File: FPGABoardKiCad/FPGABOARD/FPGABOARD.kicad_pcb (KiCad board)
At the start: 2 copper layers, 1 part, among them U1 ICE40HX1K-VQ100

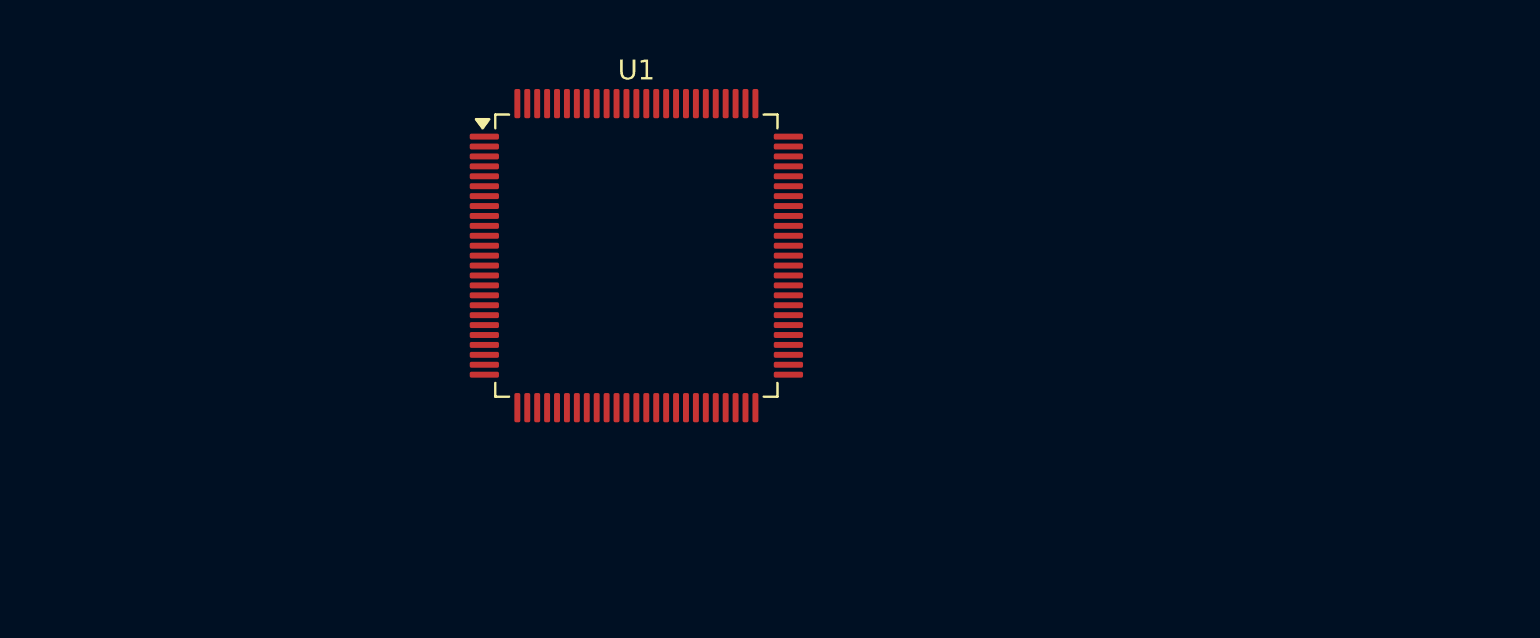
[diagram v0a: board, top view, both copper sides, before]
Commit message: FT2232 Wiring
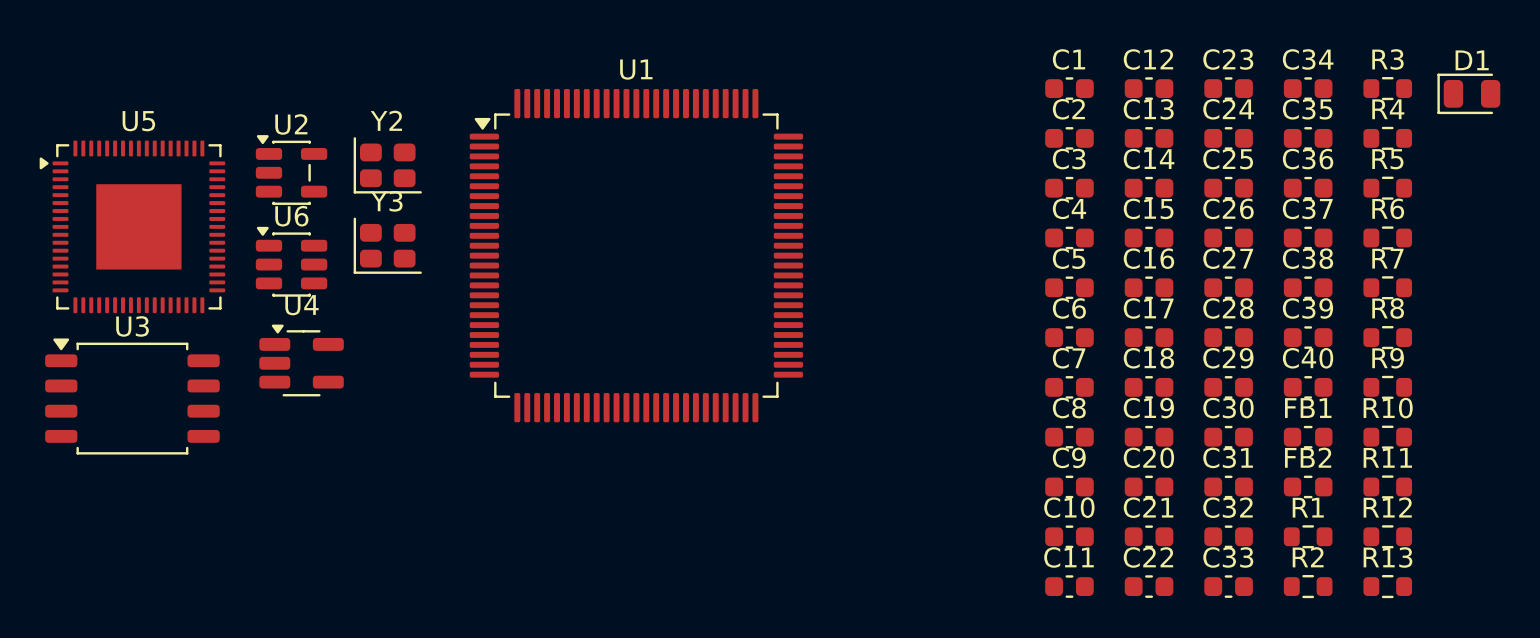
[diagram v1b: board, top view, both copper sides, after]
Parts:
- added C1: 4.7u, Capacitor_SMD:C_0603_1608Metric, F.Cu at (187.4, 94.6)
- added C10: 100n, Capacitor_SMD:C_0603_1608Metric, F.Cu at (187.4, 117.1)
- added C11: 100n, Capacitor_SMD:C_0603_1608Metric, F.Cu at (187.4, 119.7)
- added C12: 100n, Capacitor_SMD:C_0603_1608Metric, F.Cu at (191.4, 94.6)
- added C13: 10u, Capacitor_SMD:C_0603_1608Metric, F.Cu at (191.4, 97.1)
- added C14: 100n, Capacitor_SMD:C_0603_1608Metric, F.Cu at (191.4, 99.6)
- added C15: 100n, Capacitor_SMD:C_0603_1608Metric, F.Cu at (191.4, 102.1)
- added C16: 100n, Capacitor_SMD:C_0603_1608Metric, F.Cu at (191.4, 104.6)
- added C17: 100n, Capacitor_SMD:C_0603_1608Metric, F.Cu at (191.4, 107.1)
- added C18: 100n, Capacitor_SMD:C_0603_1608Metric, F.Cu at (191.4, 109.6)
- added C19: 100n, Capacitor_SMD:C_0603_1608Metric, F.Cu at (191.4, 112.1)
- added C2: 4.7u, Capacitor_SMD:C_0603_1608Metric, F.Cu at (187.4, 97.1)
- added C20: 100n, Capacitor_SMD:C_0603_1608Metric, F.Cu at (191.4, 114.6)
- added C21: 100n, Capacitor_SMD:C_0603_1608Metric, F.Cu at (191.4, 117.1)
- added C22: 100n, Capacitor_SMD:C_0603_1608Metric, F.Cu at (191.4, 119.7)
- added C23: 10u, Capacitor_SMD:C_0603_1608Metric, F.Cu at (195.4, 94.6)
- added C24: 10u, Capacitor_SMD:C_0603_1608Metric, F.Cu at (195.4, 97.1)
- added C25: 100n, Capacitor_SMD:C_0603_1608Metric, F.Cu at (195.4, 99.6)
- added C26: 100n, Capacitor_SMD:C_0603_1608Metric, F.Cu at (195.4, 102.1)
- added C27: 100n, Capacitor_SMD:C_0603_1608Metric, F.Cu at (195.4, 104.6)
- added C28: 100n, Capacitor_SMD:C_0603_1608Metric, F.Cu at (195.4, 107.1)
- added C29: 100n, Capacitor_SMD:C_0603_1608Metric, F.Cu at (195.4, 109.6)
- added C3: 4.7u, Capacitor_SMD:C_0603_1608Metric, F.Cu at (187.4, 99.6)
- added C30: 100n, Capacitor_SMD:C_0603_1608Metric, F.Cu at (195.4, 112.1)
- added C31: 100n, Capacitor_SMD:C_0603_1608Metric, F.Cu at (195.4, 114.6)
- added C32: 100n, Capacitor_SMD:C_0603_1608Metric, F.Cu at (195.4, 117.1)
- added C33: 100n, Capacitor_SMD:C_0603_1608Metric, F.Cu at (195.4, 119.7)
- added C34: 100n, Capacitor_SMD:C_0603_1608Metric, F.Cu at (199.4, 94.6)
- added C35: 10u, Capacitor_SMD:C_0603_1608Metric, F.Cu at (199.4, 97.1)
- added C36: 100n, Capacitor_SMD:C_0603_1608Metric, F.Cu at (199.4, 99.6)
- added C37: 100n, Capacitor_SMD:C_0603_1608Metric, F.Cu at (199.4, 102.1)
- added C38: 100n, Capacitor_SMD:C_0603_1608Metric, F.Cu at (199.4, 104.6)
- added C39: 100n, Capacitor_SMD:C_0603_1608Metric, F.Cu at (199.4, 107.1)
- added C4: 4.7u, Capacitor_SMD:C_0603_1608Metric, F.Cu at (187.4, 102.1)
- added C40: 10u, Capacitor_SMD:C_0603_1608Metric, F.Cu at (199.4, 109.6)
- added C5: 10u, Capacitor_SMD:C_0603_1608Metric, F.Cu at (187.4, 104.6)
- added C6: 100n, Capacitor_SMD:C_0603_1608Metric, F.Cu at (187.4, 107.1)
- added C7: 100n, Capacitor_SMD:C_0603_1608Metric, F.Cu at (187.4, 109.6)
- added C8: 100n, Capacitor_SMD:C_0603_1608Metric, F.Cu at (187.4, 112.1)
- added C9: 100n, Capacitor_SMD:C_0603_1608Metric, F.Cu at (187.4, 114.6)
- added D1: DONE, LED_SMD:LED_0805_2012Metric, F.Cu at (207.7, 94.8)
- added FB1: 60@100, Inductor_SMD:L_0603_1608Metric, F.Cu at (199.4, 112.1)
- added FB2: 60@100, Inductor_SMD:L_0603_1608Metric, F.Cu at (199.4, 114.6)
- added R1: 5k1, Resistor_SMD:R_0603_1608Metric, F.Cu at (199.4, 117.1)
- added R10: 2k2, Resistor_SMD:R_0603_1608Metric, F.Cu at (203.4, 112.1)
- added R11: 10k, Resistor_SMD:R_0603_1608Metric, F.Cu at (203.4, 114.6)
- added R12: 10k, Resistor_SMD:R_0603_1608Metric, F.Cu at (203.4, 117.1)
- added R13: 12k, Resistor_SMD:R_0603_1608Metric, F.Cu at (203.4, 119.7)
- added R2: 5k1, Resistor_SMD:R_0603_1608Metric, F.Cu at (199.4, 119.7)
- added R3: 5k1, Resistor_SMD:R_0603_1608Metric, F.Cu at (203.4, 94.6)
- added R4: 10k, Resistor_SMD:R_0603_1608Metric, F.Cu at (203.4, 97.1)
- added R5: 10k, Resistor_SMD:R_0603_1608Metric, F.Cu at (203.4, 99.6)
- added R6: 10k, Resistor_SMD:R_0603_1608Metric, F.Cu at (203.4, 102.1)
- added R7: 10k, Resistor_SMD:R_0603_1608Metric, F.Cu at (203.4, 104.6)
- added R8: 1k, Resistor_SMD:R_0603_1608Metric, F.Cu at (203.4, 107.1)
- added R9: 10k, Resistor_SMD:R_0603_1608Metric, F.Cu at (203.4, 109.6)
- added U2: AP2127K-3.3, Package_TO_SOT_SMD:SOT-23-5, F.Cu at (148.2, 98.8)
- added U3: W25Q32JVSS, Package_SO:SOIC-8_5.3x5.3mm_P1.27mm, F.Cu at (140.2, 110.2)
- added U4: AP2127K-1.2, Package_TO_SOT_SMD:SOT-23-5_HandSoldering, F.Cu at (148.7, 108.4)
- added U5: FT2232HPQ, Package_DFN_QFN:VQFN-68-1EP_8x8mm_P0.4mm_EP4.3x4.3mm, F.Cu at (140.5, 101.5)
- added U6: 93LCxxBxxOT, Package_TO_SOT_SMD:SOT-23-6, F.Cu at (148.2, 103.4)
- added Y2: SG-210STF, Oscillator:Oscillator_SMD_SeikoEpson_SG210-4Pin_2.5x2.0mm, F.Cu at (153.0, 98.4)
- added Y3: SG-210STF, Oscillator:Oscillator_SMD_SeikoEpson_SG210-4Pin_2.5x2.0mm, F.Cu at (153.0, 102.5)
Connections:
- U1 pad 11: unconnected-(U1-VCC-Pad11) -> +1V2
- U1 pad 14: unconnected-(U1-VCCIO_3__1-Pad14) -> +3V3
- U1 pad 22: unconnected-(U1-VCCIO_3__2-Pad22) -> +3V3
- U1 pad 31: unconnected-(U1-VCCIO_2-Pad31) -> +3V3
- U1 pad 35: unconnected-(U1-VCC__1-Pad35) -> +1V2
- U1 pad 38: unconnected-(U1-VCCIO_2__1-Pad38) -> +3V3
- U1 pad 43: unconnected-(U1-CDONE-Pad43) -> /CDONE
- U1 pad 44: unconnected-(U1-CRESET_B-Pad44) -> /CRESET_B
- U1 pad 45: unconnected-(U1-IOB_44_SDO-Pad45) -> /ICE_SDO
- U1 pad 46: unconnected-(U1-IOB_45_SDI-Pad46) -> /ICE_SDI
- U1 pad 48: unconnected-(U1-IOB_46_SCK-Pad48) -> /ICE_SCK
- U1 pad 49: unconnected-(U1-IOB_47_SS-Pad49) -> /ICE_SS
- U1 pad 50: unconnected-(U1-VCC_SPI-Pad50) -> +3V3
- U1 pad 58: unconnected-(U1-VCCIO_1-Pad58) -> +3V3
- U1 pad 6: unconnected-(U1-VCCIO_3-Pad6) -> +3V3
- U1 pad 61: unconnected-(U1-VCC__2-Pad61) -> +1V2
- U1 pad 67: unconnected-(U1-VCCIO_1__1-Pad67) -> +3V3
- U1 pad 75: unconnected-(U1-VPP_2V5-Pad75) -> +3V3
- U1 pad 77: unconnected-(U1-VCC__3-Pad77) -> +1V2
- U1 pad 88: unconnected-(U1-VCCIO_0-Pad88) -> +3V3
- U1 pad 90: unconnected-(U1-IOT_85_GBIN0-Pad90) -> /ICE_CLOCK0
- U1 pad 92: unconnected-(U1-VCCIO_0__1-Pad92) -> +3V3

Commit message: Update IO
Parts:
- added C41: 100n, Capacitor_SMD:C_0603_1608Metric, F.Cu at (184.5, 102.5)
- added C42: 100n, Capacitor_SMD:C_0603_1608Metric, F.Cu at (184.5, 105.0)
- added D2: PWRSTATUS, LED_SMD:LED_01005_0402Metric, F.Cu at (190.2, 131.9)
- added D3: LED0, LED_SMD:LED_01005_0402Metric, F.Cu at (190.2, 133.5)
- added D4: LED1, LED_SMD:LED_01005_0402Metric, F.Cu at (190.2, 135.2)
- added D5: LED2, LED_SMD:LED_01005_0402Metric, F.Cu at (190.2, 136.8)
- added J1: USB_C_Receptacle_USB2.0_14P, Connector_USB:USB_C_Receptacle_G-Switch_GT-USB-7010ASV, F.Cu at (207.5, 133.6)
- added J2: 12PMOD, Connector_PinSocket_2.54mm:PinSocket_2x06_P2.54mm_Horizontal, F.Cu at (223.1, 93.5)
- added J3: Conn_02x12_Odd_Even, Connector_PinSocket_2.54mm:PinSocket_2x12_P2.54mm_Vertical, F.Cu at (199.4, 113.2)
- added J4: 6PMOD, Connector_PinSocket_2.54mm:PinSocket_1x06_P2.54mm_Horizontal, F.Cu at (212.8, 113.2)
- added J5: I2C, Connector_PinSocket_2.54mm:PinSocket_1x04_P2.54mm_Vertical, F.Cu at (217.3, 113.2)
- added R14: 10k, Resistor_SMD:R_0603_1608Metric, F.Cu at (188.5, 115.0)
- added R15: 10k, Resistor_SMD:R_0603_1608Metric, F.Cu at (188.5, 117.6)
- added R16: 10k, Resistor_SMD:R_0603_1608Metric, F.Cu at (188.5, 120.1)
- added R17: 10k, Resistor_SMD:R_0603_1608Metric, F.Cu at (192.6, 92.5)
- added R18: 2k2, Resistor_SMD:R_0603_1608Metric, F.Cu at (192.6, 95.0)
- added R19: 10k, Resistor_SMD:R_0603_1608Metric, F.Cu at (192.6, 97.5)
- added R20: 10k, Resistor_SMD:R_0603_1608Metric, F.Cu at (192.6, 100.0)
- added R21: 10k, Resistor_SMD:R_0603_1608Metric, F.Cu at (192.6, 102.5)
- added R22: 2k2, Resistor_SMD:R_0603_1608Metric, F.Cu at (192.6, 105.0)
- added U7: IS62LV256AL, Package_SO:SOP-28_8.4x18.16mm_P1.27mm, F.Cu at (202.0, 101.1)
- D1: footprint LED_SMD:LED_0805_2012Metric -> LED_SMD:LED_01005_0402Metric
- R9: value 10k -> 5k1
- moved U5 84.6 mm to (218.9, 133.3)
- moved U2 75.4 mm to (222.2, 113.3)
- moved U6 75.4 mm to (222.2, 117.9)
- moved U4 75.0 mm to (216.3, 140.9)
- moved U3 73.8 mm to (206.9, 141.8)
- moved Y2 45.5 mm to (191.1, 123.3)
- moved Y3 45.5 mm to (191.1, 127.4)
- moved D1 39.5 mm to (190.2, 130.2)
- moved C12 31.8 mm to (172.5, 120.1)
- moved U1 30.9 mm to (179.7, 130.5)
- moved C23 29.8 mm to (176.5, 117.6)
- moved C24 29.8 mm to (176.5, 120.1)
- moved R3 29.8 mm to (184.5, 117.6)
- moved R4 29.8 mm to (184.5, 120.1)
- moved C35 27.9 mm to (180.5, 117.6)
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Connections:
- U5 pad 34: unconnected-(U5-BDBUS0-Pad34) -> /ICERX
- U5 pad 35: unconnected-(U5-BDBUS1-Pad35) -> /ICETX

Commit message: Some placements
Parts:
- removed C35, C40: 10u, Capacitor_SMD:C_0603_1608Metric
- added SW1: ResetICE, Button_Switch_SMD:SW_SPST_PTS647_Sx50, F.Cu at (233.7, 147.6)
- added SW2: BTN0, Button_Switch_SMD:SW_SPST_PTS647_Sx50, F.Cu at (222.8, 118.3)
- added SW3: BTN1, Button_Switch_SMD:SW_SPST_PTS647_Sx50, F.Cu at (222.8, 124.8)
- added SW4: BTN2, Button_Switch_SMD:SW_SPST_PTS647_Sx50, F.Cu at (222.8, 131.2)
- C1, C2, C25, C26, C27, C28, C29, C3, C30, C31, C32, C33, C34, C36, C37, C4, C41, C42, C5, C6, C7, C8: footprint Capacitor_SMD:C_0603_1608Metric -> Capacitor_SMD:C_0805_2012Metric
- C10, C11, C12, C13, C14, C15, C16, C17, C18, C19, C20, C21, C22, C23, C24, C38, C39, C9: footprint Capacitor_SMD:C_0603_1608Metric -> Capacitor_SMD:C_0805_2012Metric; moved to B.Cu
- D1, D2, D3, D4, D5: footprint LED_SMD:LED_01005_0402Metric -> LED_SMD:LED_1206_3216Metric
- FB1, FB2: footprint Inductor_SMD:L_0603_1608Metric -> Inductor_SMD:L_0805_2012Metric
- R1, R10, R11, R13, R14, R15, R16, R17, R18, R19, R2, R20, R21, R22, R3, R4, R5, R6, R7, R8, R9: footprint Resistor_SMD:R_0603_1608Metric -> Resistor_SMD:R_0805_2012Metric
- R12: footprint Resistor_SMD:R_0603_1608Metric -> Resistor_SMD:R_0805_2012Metric; moved to B.Cu
- U2: footprint Package_TO_SOT_SMD:SOT-23-5 -> Package_TO_SOT_SMD:SOT-23-5_HandSoldering
- moved U2 128.7 mm to (98.0, 79.5)
- moved J1 127.1 mm to (85.0, 100.0), turned to -90 degrees
- moved C38 122.7 mm to (63.8, 73.2), turned to 180 degrees
- moved C39 122.7 mm to (63.8, 75.7), turned to 180 degrees
- moved U5 121.5 mm to (102.0, 100.2), turned to 90 degrees
- moved U4 119.1 mm to (114.2, 79.5)
- moved U6 110.9 mm to (115.2, 147.1), turned to 90 degrees
- moved C30 110.4 mm to (73.5, 78.2)
- moved C31 110.4 mm to (73.5, 80.7)
- moved C32 110.4 mm to (73.5, 83.2)
- moved R1 100.0 mm to (86.4, 93.0)
- moved R2 98.5 mm to (86.4, 107.0), turned to 180 degrees
- moved R3 95.2 mm to (96.0, 82.5)
- moved R13 94.5 mm to (94.7, 101.0)
- moved FB2 93.1 mm to (91.8, 102.2), turned to 90 degrees
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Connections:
- C37 pad 1: unconnected-(C37-Pad1) -> +1V2
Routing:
- net /D-: track 0.00 -> 11.9 mm
- net /D+: track 0.00 -> 11.9 mm
- net Net-(U5-VCC_PD): track 0.00 -> 10.4 mm
- net Net-(U5-VCC_USB): track 0.00 -> 5.14 mm
- net +1V2: track 0.00 -> 4.17 mm
- net Net-(U5-REF): track 0.00 -> 3.23 mm
- net +3V3: track 0.00 -> 2.79 mm
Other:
- copper layers 2 -> 4
- rule pad_to_mask_clearance: 0 -> 0.05

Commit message: More pcb work
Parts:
- moved D1 182.9 mm to (82.0, 86.1)
- moved D2 182.9 mm to (89.0, 86.1)
- moved R14 182.9 mm to (89.0, 80.7)
- moved R8 182.9 mm to (81.9, 80.9)
- moved SW1 153.8 mm to (83.8, 112.9), turned to 90 degrees
- moved R9 148.1 mm to (82.0, 119.0), turned to 90 degrees
- moved C41 146.3 mm to (85.2, 118.3), turned to 0 degrees
- moved C25 57.3 mm to (112.8, 95.2), turned to 180 degrees
- moved Y3 51.7 mm to (112.8, 98.2), turned to 180 degrees
- moved C26 50.7 mm to (109.6, 98.0), turned to 90 degrees
- moved R11 46.0 mm to (90.9, 109.0), turned to 180 degrees
- moved C27 45.0 mm to (91.0, 106.5)
- moved R10 44.7 mm to (95.0, 110.9)
- moved U6 44.5 mm to (95.0, 107.5)
- moved C37 25.2 mm to (101.6, 67.2)
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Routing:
- net +1V2: track 4.17 -> 0.00 mm
- net +3V3: track 2.79 -> 0.00 mm
- net Net-(U5-VCC_USB): track 5.14 -> 3.14 mm
- net /D-: track 11.9 -> 13.0 mm
- net /D+: track 11.9 -> 12.9 mm

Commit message: More placements
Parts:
- moved D3 145.1 mm to (99.5, 91.8)
- moved D4 145.1 mm to (104.0, 91.7)
- moved D5 145.1 mm to (108.1, 91.6)
- moved R19 145.1 mm to (99.5, 86.5)
- moved R20 145.1 mm to (104.0, 86.4)
- moved R21 145.1 mm to (108.0, 86.4)
- moved R22 136.1 mm to (82.7, 124.4), turned to 180 degrees
- moved R18 132.8 mm to (89.6, 124.1)
- moved R17 131.8 mm to (96.2, 129.8), turned to 0 degrees
- moved SW4 127.4 mm to (95.6, 124.6), turned to -90 degrees
- moved R16 125.2 mm to (102.9, 129.8), turned to 0 degrees
- moved SW3 120.7 mm to (102.0, 124.6), turned to -90 degrees
- moved R15 119.2 mm to (109.4, 129.8), turned to 0 degrees
- moved SW2 114.4 mm to (108.5, 124.6), turned to -90 degrees
- moved R7 100.5 mm to (98.5, 114.1), turned to 90 degrees
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
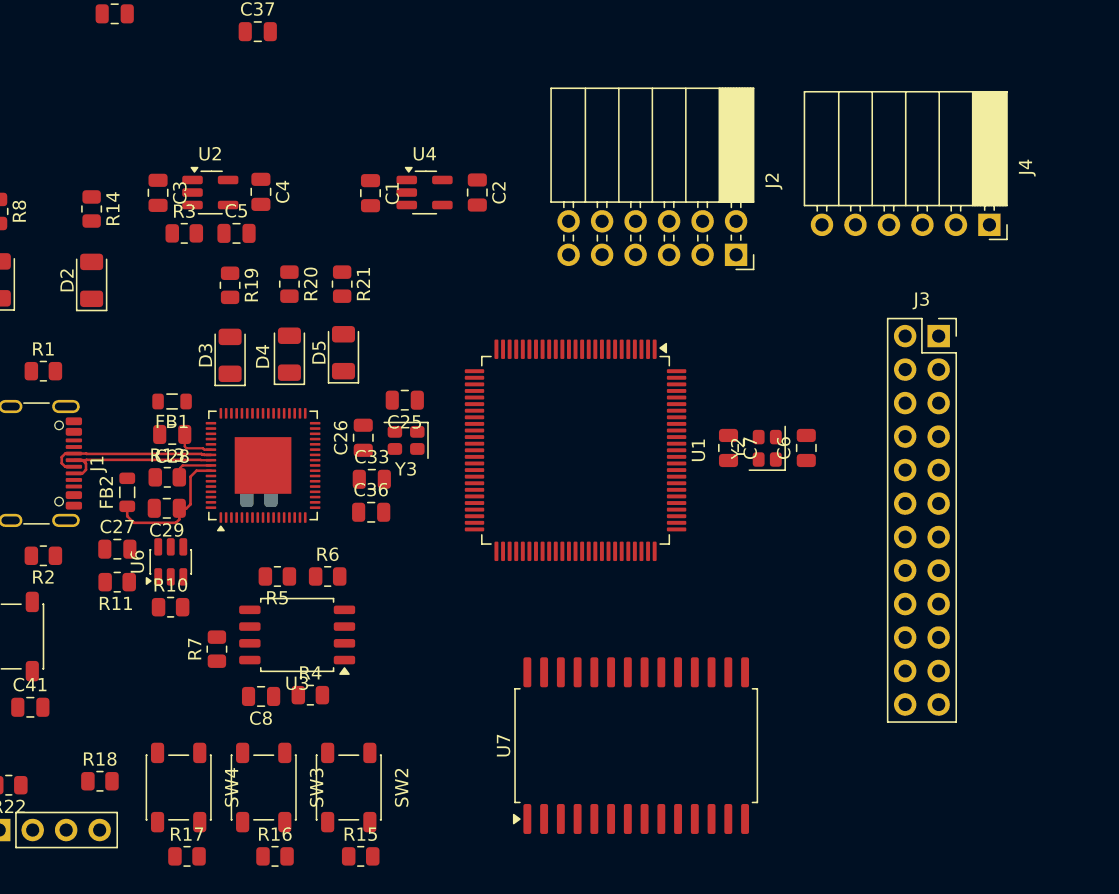
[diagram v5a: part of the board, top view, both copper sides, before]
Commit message: Finished placements mostly
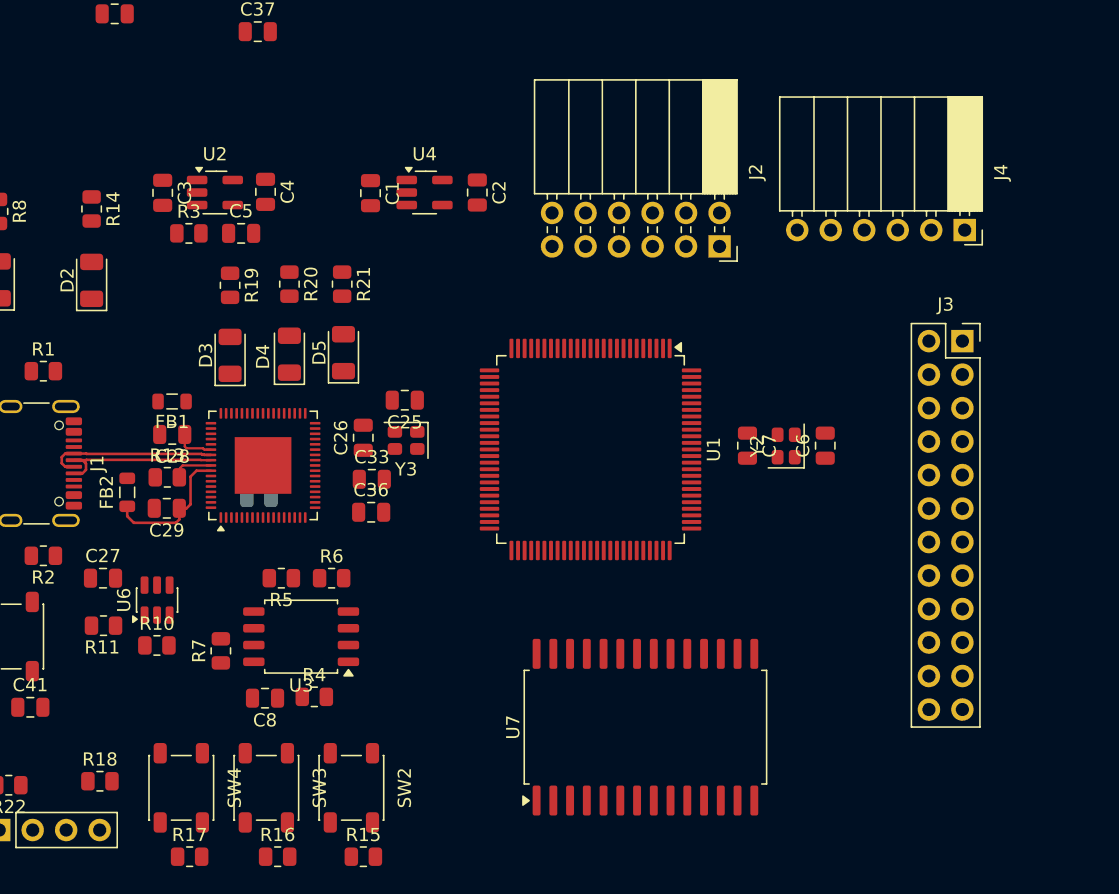
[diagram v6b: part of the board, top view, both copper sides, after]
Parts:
- moved R11 3.46 mm to (89.9, 112.3)
- moved R10 3.08 mm to (94.0, 113.8)
- moved U6 3.08 mm to (94.0, 110.4)
- moved C27 2.45 mm to (89.9, 108.7)
- moved J4 1.92 mm to (155.2, 82.3)
- moved J3 1.84 mm to (155.0, 90.7)
- moved U7 1.57 mm to (131.0, 120.0)
- moved C6 1.45 mm to (144.6, 98.7)
- moved C7 1.45 mm to (138.7, 98.7)
- moved Y2 1.45 mm to (141.7, 98.7)
- moved J2 1.41 mm to (136.6, 83.5)
- moved U1 1.14 mm to (126.8, 98.9)
- moved C3 0.35 mm to (94.4, 79.5)
- moved C5 0.35 mm to (100.3, 82.5)
- moved C4 0.35 mm to (102.2, 79.4)
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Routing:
- added copper zone on In2.Cu, net +1V2
